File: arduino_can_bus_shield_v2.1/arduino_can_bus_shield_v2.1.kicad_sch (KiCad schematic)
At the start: 32 parts, among them J1 Power, J2 Digital/PWM, J3 Analog, J4 Digital/PWM, J6 xt60 male, J7 molex_3.0, M1 MPU9250_module, SW1 User, SW2 User, SW3 SW_DIP_x04, U1 MP1584, U2 MCP2551-I-SN, U3 MCP2515-xST, Y1 16MHz

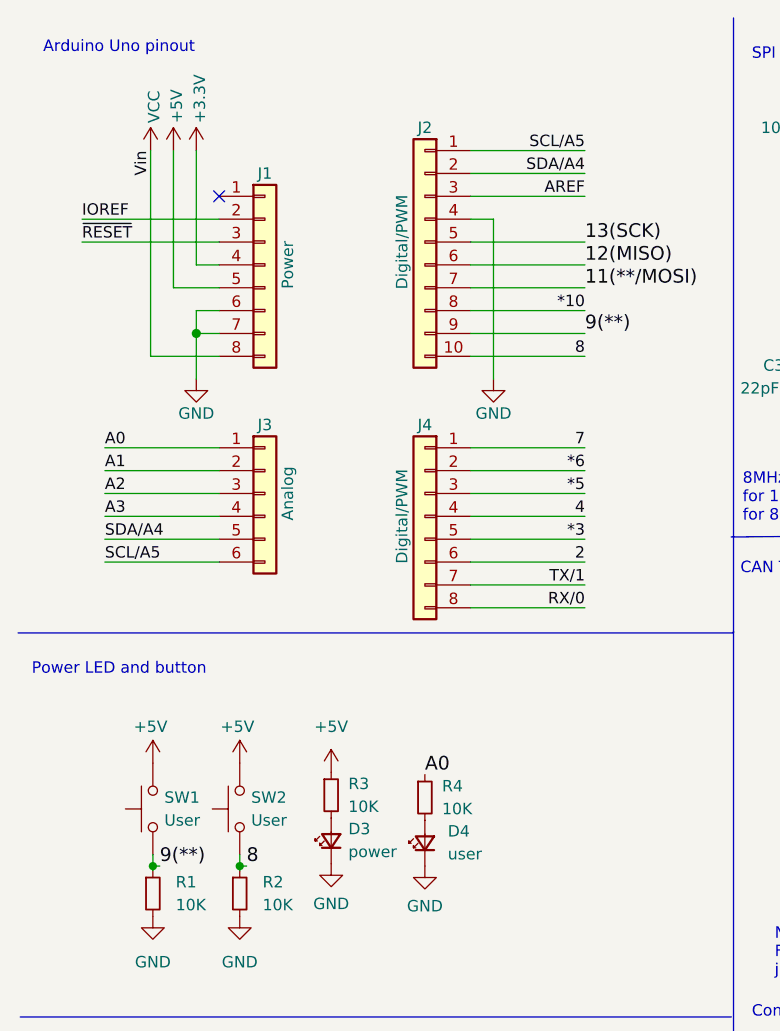
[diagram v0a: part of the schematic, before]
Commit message: fixed pin 9 button to pin 6
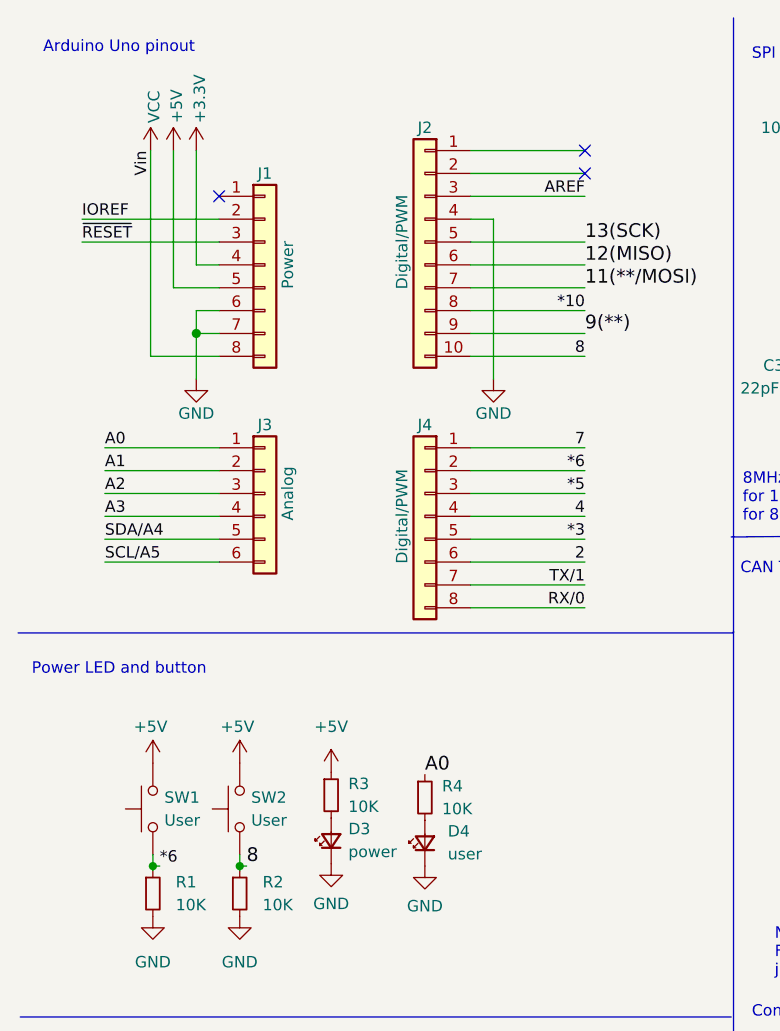
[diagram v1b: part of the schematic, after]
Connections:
- net *6: now also R1.1, SW1.1
- net 9(**): no longer R1.1, SW1.1
- net SCL/A5: no longer J2.1 (Pin_1)
- net SDA/A4: no longer J2.2 (Pin_2)
- no-connect marks 16 -> 18
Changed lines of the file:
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@@
   (no_connect (at 118.364 137.922))
   (no_connect (at 117.094 184.404))
+  (no_connect (at 74.93 26.67))
+  (no_connect (at 74.93 29.21))
   (no_connect (at 105.156 94.488))
   (no_connect (at 149.86 51.816))
@@
     (effects (font (size 1.27 1.27)) (justify left bottom))
   )
+  (label "*6" (at 27.686 106.172 0)
+    (effects (font (size 1.27 1.27)) (justify left bottom))
+  )
   (label "13(SCK)" (at 74.93 36.83 0)
     (effects (font (size 1.524 1.524)) (justify left bottom))
@@
     (effects (font (size 1.27 1.27)) (justify right bottom))
   )
-  (label "SDA{slash}A4" (at 74.93 29.21 180)
-    (effects (font (size 1.27 1.27)) (justify right bottom))
-  )
   (label "8" (at 74.93 49.53 180)
     (effects (font (size 1.27 1.27)) (justify right bottom))
@@
     (effects (font (size 1.27 1.27)) (justify right bottom))
   )
-  (label "SCL{slash}A5" (at 74.93 26.67 180)
-    (effects (font (size 1.27 1.27)) (justify right bottom))
-  )
   (label "CAN-" (at 105.664 140.462 180)
     (effects (font (size 1.27 1.27)) (justify right bottom))
@@
     (effects (font (size 1.27 1.27)) (justify right bottom))
   )
-  (label "9(**)" (at 27.686 106.172 0)
-    (effects (font (size 1.524 1.524)) (justify left bottom))
-  )
   (symbol (lib_id "Connector_Generic:Conn_01x08") (at 39.37 39.37 0) (unit 1)
